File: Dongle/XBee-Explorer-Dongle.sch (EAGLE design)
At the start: 33 parts, among them U2 XBEE-1B3, U3 MIC5205 3.3V, U4 FT231XS

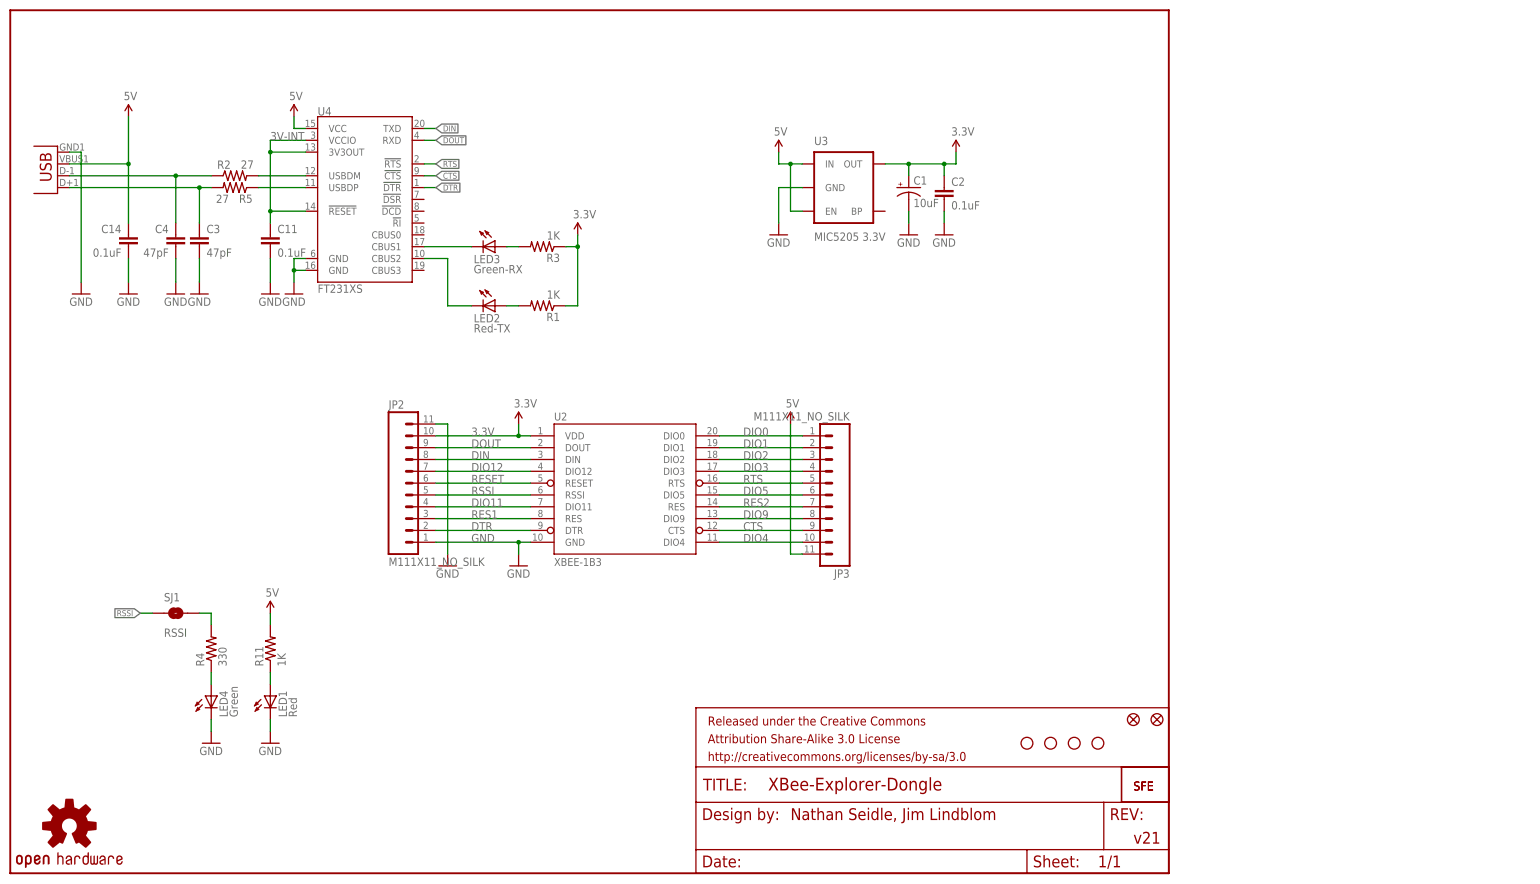
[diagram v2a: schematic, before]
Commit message: Adding reset button, jumpers on UART ctrl lines
Reset button required moving LEDs around.
Adding jumpers on DTR, CTS, and RTS because they're not present on some
XBee compatible boards. Those pins can be used as GPIOs.
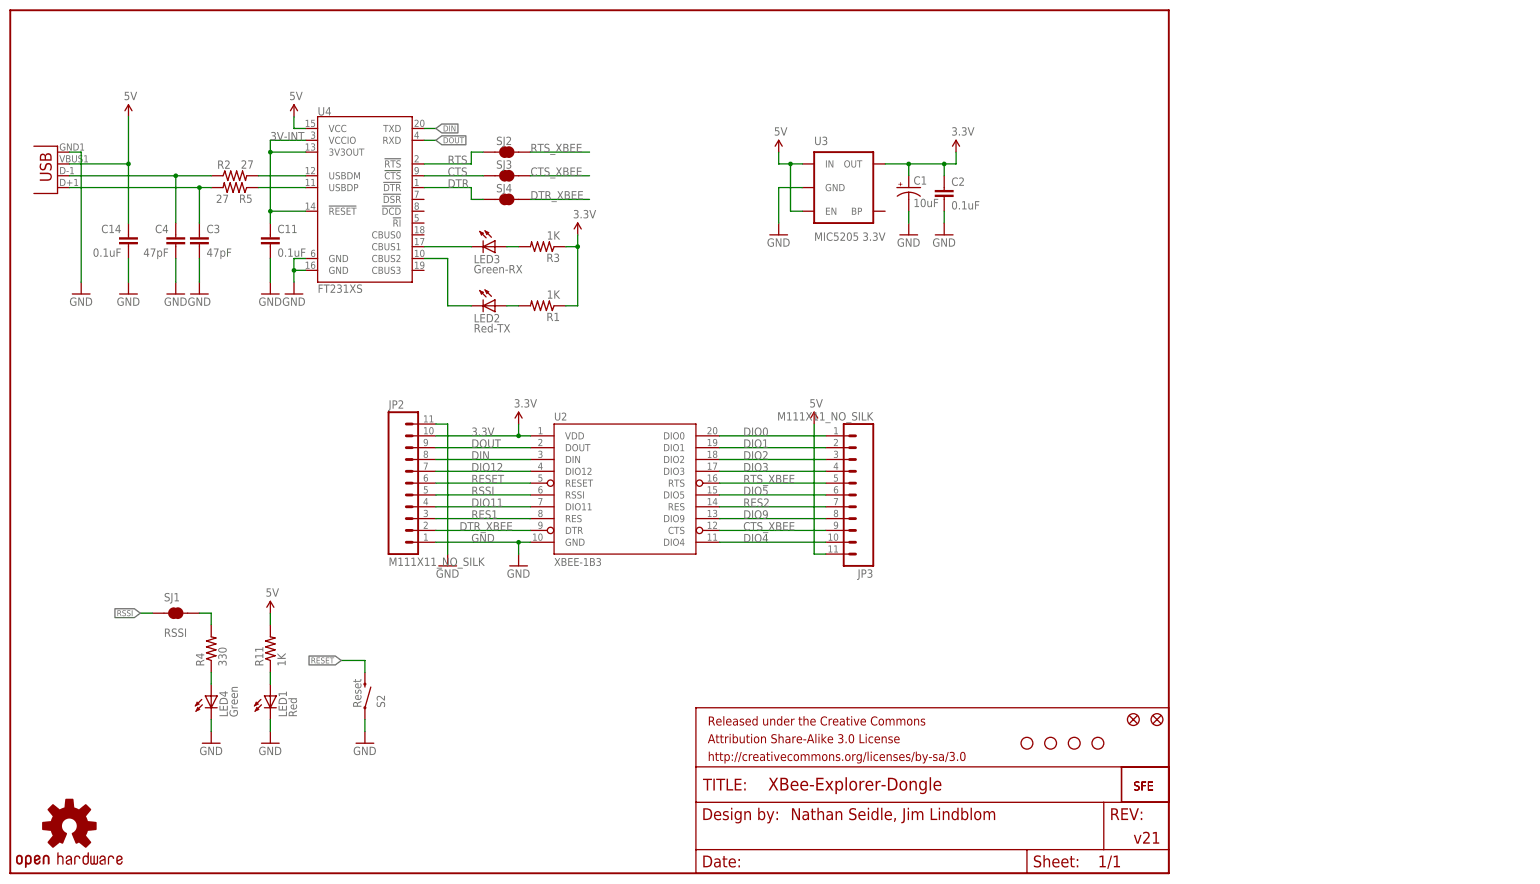
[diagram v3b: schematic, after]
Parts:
- added S2: Reset, SparkFun-Electromechanical:SWITCH-MOMENTARY-2SMD
- added SJ2, SJ3, SJ4: RSSI, SparkFun-Passives:SOLDERJUMPERTRACE
- U2: device SparkFun:XBEE-1B3 -> SparkFun-RF:XBEE-1B3
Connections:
- new net CTS_XBEE: JP3.9, SJ3.2, U2.CTS
- new net DTR_XBEE: JP2.2, SJ4.2, U2.DTR
- new net RTS_XBEE: JP3.5, SJ2.2, U2.RTS
- net CTS: now also SJ3.1; no longer JP3.9, U2.CTS
- net DTR: now also SJ4.1; no longer JP2.2, U2.DTR
- net GND: now also S2.1
- net RESET: now also S2.2
- net RTS: now also SJ2.1; no longer JP3.5, U2.RTS
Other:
- moved on the sheet: JP3

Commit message: Increasing fiducial size and LED footprint
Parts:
- removed LED1: Red, SparkFun:LED0603
- removed LED2: Red-TX, SparkFun:LED0603
- removed LED3: Green-RX, SparkFun:LED0603
- removed LED4: Green, SparkFun:LED0603
- added D1, D4: RED, SparkFun-LED:LED-RED0603
- added D2, D3: GREEN, SparkFun-LED:LED-GREEN0603
- FID1, FID2: value FIDUCIALUFIDUCIAL -> FIDUCIAL1X2; device SparkFun-Aesthetics:FIDUCIALUFIDUCIAL -> SparkFun-Aesthetics:FIDUCIAL1X2
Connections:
- net GND: now also D3.C, D4.C; no longer LED1.C, LED4.C
- net N$1: now also D1.A; no longer LED2.A
- net N$2: now also D3.A; no longer LED4.A
- net N$38: now also D4.A; no longer LED1.A
- net N$4: now also D2.A; no longer LED3.A
- net RXLED: now also D2.C; no longer LED3.C
- net TXLED: now also D1.C; no longer LED2.C

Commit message: Updating USB dongle connector to use locking fp
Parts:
- JP1: value USBA-SMD-MALE -> USBA-SMD-MALE-LOCKING; device SparkFun-Connectors:USBA-SMD-MALE -> SparkFun-Connectors:USBA-SMD-MALE-LOCKING
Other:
- note added: "v22"
- note removed: "v21"
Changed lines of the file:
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@@
 <grid distance="0.1" unitdist="inch" unit="inch" style="lines" multiple="1" display="no" altdistance="0.01" altunitdist="inch" altunit="inch"/>
 <layers>
-<layer number="1" name="Top" color="4" fill="1" visible="no" active="no"/>
-<layer number="2" name="Route2" color="1" fill="3" visible="no" active="no"/>
-<layer number="3" name="Route3" color="4" fill="3" visible="no" active="no"/>
-<layer number="4" name="Route4" color="1" fill="4" visible="no" active="no"/>
-<layer number="5" name="Route5" color="4" fill="4" visible="no" active="no"/>
-<layer number="6" name="Route6" color="1" fill="8" visible="no" active="no"/>
-<layer number="7" name="Route7" color="4" fill="8" visible="no" active="no"/>
-<layer number="8" name="Route8" color="1" fill="2" visible="no" active="no"/>
-<layer number="9" name="Route9" color="4" fill="2" visible="no" active="no"/>
-<layer number="10" name="Route10" color="1" fill="7" visible="no" active="no"/>
-<layer number="11" name="Route11" color="4" fill="7" visible="no" active="no"/>
-<layer number="12" name="Route12" color="1" fill="5" visible="no" active="no"/>
-<layer number="13" name="Route13" color="4" fill="5" visible="no" active="no"/>
-<layer number="14" name="Route14" color="1" fill="6" visible="no" active="no"/>
-<layer number="15" name="Route15" color="4" fill="6" visible="no" active="no"/>
-<layer number="16" name="Bottom" color="1" fill="1" visible="no" active="no"/>
-<layer number="17" name="Pads" color="2" fill="1" visible="no" active="no"/>
-<layer number="18" name="Vias" color="2" fill="1" visible="no" active="no"/>
-<layer number="19" name="Unrouted" color="6" fill="1" visible="no" active="no"/>
-<layer number="20" name="Dimension" color="15" fill="1" visible="no" active="no"/>
-<layer number="21" name="tPlace" color="16" fill="1" visible="no" active="no"/>
-<layer number="22" name="bPlace" color="14" fill="1" visible="no" active="no"/>
-<layer number="23" name="tOrigins" color="15" fill="1" visible="no" active="no"/>
-<layer number="24" name="bOrigins" color="15" fill="1" visible="no" active="no"/>
-<layer number="25" name="tNames" color="7" fill="1" visible="no" active="no"/>
-<layer number="26" name="bNames" color="7" fill="1" visible="no" active="no"/>
-<layer number="27" name="tValues" color="7" fill="1" visible="no" active="no"/>
-<layer number="28" name="bValues" color="7" fill="1" visible="no" active="no"/>
+<layer number="1" name="Top" color="4" fill="1" visible="yes" active="no"/>
+<layer number="2" name="Route2" color="1" fill="3" visible="yes" active="no"/>
+<layer number="3" name="Route3" color="4" fill="3" visible="yes" active="no"/>
+<layer number="4" name="Route4" color="1" fill="4" visible="yes" active="no"/>
+<layer number="5" name="Route5" color="4" fill="4" visible="yes" active="no"/>
+<layer number="6" name="Route6" color="1" fill="8" visible="yes" active="no"/>
+<layer number="7" name="Route7" color="4" fill="8" visible="yes" active="no"/>
+<layer number="8" name="Route8" color="1" fill="2" visible="yes" active="no"/>
+<layer number="9" name="Route9" color="4" fill="2" visible="yes" active="no"/>
+<layer number="10" name="Route10" color="1" fill="7" visible="yes" active="no"/>
+<layer number="11" name="Route11" color="4" fill="7" visible="yes" active="no"/>
+<layer number="12" name="Route12" color="1" fill="5" visible="yes" active="no"/>
+<layer number="13" name="Route13" color="4" fill="5" visible="yes" active="no"/>
+<layer number="14" name="Route14" color="1" fill="6" visible="yes" active="no"/>
+<layer number="15" name="Route15" color="4" fill="6" visible="yes" active="no"/>
+<layer number="16" name="Bottom" color="1" fill="1" visible="yes" active="no"/>
+<layer number="17" name="Pads" color="2" fill="1" visible="yes" active="no"/>
+<layer number="18" name="Vias" color="2" fill="1" visible="yes" active="no"/>
+<layer number="19" name="Unrouted" color="6" fill="1" visible="yes" active="no"/>
+<layer number="20" name="Dimension" color="15" fill="1" visible="yes" active="no"/>
+<layer number="21" name="tPlace" color="16" fill="1" visible="yes" active="no"/>
+<layer number="22" name="bPlace" color="14" fill="1" visible="yes" active="no"/>
+<layer number="23" name="tOrigins" color="15" fill="1" visible="yes" active="no"/>
+<layer number="24" name="bOrigins" color="15" fill="1" visible="yes" active="no"/>
+<layer number="25" name="tNames" color="7" fill="1" visible="yes" active="no"/>
+<layer number="26" name="bNames" color="7" fill="1" visible="yes" active="no"/>
+<layer number="27" name="tValues" color="7" fill="1" visible="yes" active="no"/>
+<layer number="28" name="bValues" color="7" fill="1" visible="yes" active="no"/>
 <layer number="29" name="tStop" color="7" fill="3" visible="no" active="no"/>
 <layer number="30" name="bStop" color="7" fill="6" visible="no" active="no"/>
@@
 <layer number="35" name="tGlue" color="7" fill="4" visible="no" active="no"/>
 <layer number="36" name="bGlue" color="7" fill="5" visible="no" active="no"/>
-<layer number="37" name="tTest" color="7" fill="1" visible="no" active="no"/>
-<layer number="38" name="bTest" color="7" fill="1" visible="no" active="no"/>
+<layer number="37" name="tTest" color="7" fill="1" visible="yes" active="no"/>
+<layer number="38" name="bTest" color="7" fill="1" visible="yes" active="no"/>
 <layer number="39" name="tKeepout" color="4" fill="11" visible="no" active="no"/>
 <layer number="40" name="bKeepout" color="1" fill="11" visible="no" active="no"/>
@@
 <layer number="44" name="Drills" color="7" fill="1" visible="no" active="no"/>
 <layer number="45" name="Holes" color="7" fill="1" visible="no" active="no"/>
-<layer number="46" name="Milling" color="3" fill="1" visible="no" active="no"/>
-<layer number="47" name="Measures" color="7" fill="1" visible="no" active="no"/>
-<layer number="48" name="Document" color="7" fill="1" visible="no" active="no"/>
-<layer number="49" name="Reference" color="7" fill="1" visible="no" active="no"/>
-<layer number="50" name="dxf" color="7" fill="1" visible="no" active="no"/>
-<layer number="51" name="tDocu" color="6" fill="1" visible="no" active="no"/>
-<layer number="52" name="bDocu" color="7" fill="1" visible="no" active="no"/>
-<layer number="53" name="tGND_GNDA" color="7" fill="9" visible="no" active="no"/>
-<layer number="54" name="bGND_GNDA" color="1" fill="9" visible="no" active="no"/>
-<layer number="56" name="wert" color="7" fill="1" visible="no" active="no"/>
+<layer number="46" name="Milling" color="3" fill="1" visible="yes" active="no"/>
+<layer number="47" name="Measures" color="7" fill="1" visible="yes" active="no"/>
+<layer number="48" name="Document" color="7" fill="1" visible="yes" active="no"/>
+<layer number="49" name="Reference" color="7" fill="1" visible="yes" active="no"/>
+<layer number="50" name="dxf" color="7" fill="1" visible="yes" active="no"/>
+<layer number="51" name="tDocu" color="6" fill="1" visible="yes" active="no"/>
+<layer number="52" name="bDocu" color="7" fill="1" visible="yes" active="no"/>
+<layer number="53" name="tGND_GNDA" color="7" fill="9" visible="yes" active="no"/>
+<layer number="54" name="bGND_GNDA" color="1" fill="9" visible="yes" active="no"/>
+<layer number="56" name="wert" color="7" fill="1" visible="yes" active="no"/>
+<layer number="57" name="tCAD" color="7" fill="1" visible="yes" active="no"/>
 <layer number="91" name="Nets" color="2" fill="1" visible="yes" active="yes"/>
 <layer number="92" name="Busses" color="1" fill="1" visible="yes" active="yes"/>
@@
 <layer number="97" name="Info" color="7" fill="1" visible="yes" active="yes"/>
 <layer number="98" name="Guide" color="6" fill="1" visible="yes" active="yes"/>
+<layer number="99" name="SpiceOrder" color="7" fill="1" visible="yes" active="yes"/>
 <layer number="100" name="Muster" color="7" fill="1" visible="no" active="no"/>
 <layer number="101" name="Patch_Top" color="12" fill="4" visible="yes" active="yes"/>
@@
 <layer number="132" name="bAdjust" color="7" fill="1" visible="yes" active="yes"/>
 <layer number="144" name="Drill_legend" color="7" fill="1" visible="no" active="yes"/>
+<layer number="150" name="Notes" color="7" fill="1" visible="yes" active="yes"/>
 <layer number="151" name="HeatSink" color="7" fill="1" visible="yes" active="yes"/>
 <layer number="152" name="_bDocu" color="7" fill="1" visible="yes" active="yes"/>
+<layer number="153" name="FabDoc1" color="7" fill="1" visible="yes" active="yes"/>
+<layer number="154" name="FabDoc2" color="7" fill="1" visible="yes" active="yes"/>
+<layer number="155" name="FabDoc3" color="7" fill="1" visible="yes" active="yes"/>
 <layer number="199" name="Contour" color="7" fill="1" visible="yes" active="yes"/>
 <layer number="200" name="200bmp" color="1" fill="10" visible="no" active="no"/>
@@
 <part name="GND7" library="SparkFun" deviceset="GND" device=""/>
 <part name="U$7" library="SparkFun" deviceset="OSHW-LOGO" device="S"/>
-<part name="JP1" library="SparkFun-Connectors" deviceset="USB" device="A-SMD-MALE"/>
+<part name="JP1" library="SparkFun-Connectors" deviceset="USB" device="A-SMD-MALE-LOCKING" value="USBA-SMD-MALE-LOCKING"/>
 <part name="U4" library="SparkFun-DigitalIC" deviceset="FT231X" device="S"/>
 <part name="R2" library="SparkFun" deviceset="RESISTOR" device="0603-RES" value="27"/>
@@
 <plain>
 <text x="167.64" y="12.7" size="2.54" layer="94" align="center-left">Nathan Seidle, Jim Lindblom</text>
-<text x="241.3" y="7.62" size="2.54" layer="94" align="center-left">v21</text>
+<text x="241.3" y="7.62" size="2.54" layer="94" align="center-left">v22</text>
 <wire x1="105.664" y1="154.94" x2="107.696" y2="154.94" width="0.762" layer="94"/>
 <wire x1="105.664" y1="149.86" x2="107.696" y2="149.86" width="0.762" layer="94"/>
